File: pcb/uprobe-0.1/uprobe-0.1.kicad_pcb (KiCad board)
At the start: 4 copper layers, 33.5 x 77 mm, 103 parts, among them J1 uConsoleEXT, J2 Conn_02x05_Odd_Even, J3 Conn_02x05_Odd_Even, J4 JST_SH_BM03B-SRSS, J5 Conn_01x02, J7 Conn_01x04, Q1 BSS138, Q2 BSS138, Q3 BSS138, Q4 BSS138, Q5 BSS138, Q6 BSS138, Q7 DMG1024UV, Q8 DMG1023UV, SW1 XUNPU TS-1088-AR02016, SW2 XUNPU TS-1088-AR02016, U1 ATmega8A-M, U2 AMS1117-3.3, U3 AP22653, U4 AP22653, U5 STM32F103CBUx, U6 74LVC2T45DC, U7 74LVC2T45DC, U8 74LVC2T45DC, U9 74LVC2T45DC, Y1 ABM8-12.000MHZ-B2-T, Y2 ABM8-8.000MHZ-B2-T

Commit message: update usbasp schema
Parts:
- removed Q2, Q3, Q4, Q5, Q6: BSS138, Package_TO_SOT_SMD:SOT-23
- removed R11, R12, R13, R14, R15, R16, R17, R18, R19, R20: 10k, Resistor_SMD:R_0603_1608Metric
- removed R21, R22, R23, R24: 270, Resistor_SMD:R_0603_1608Metric
- added C29: 100n, Capacitor_SMD:C_0603_1608Metric, F.Cu at (136.7, 86.7)
- added C30: 100n, Capacitor_SMD:C_0603_1608Metric, F.Cu at (136.7, 82.5)
- added C31: 100n, Capacitor_SMD:C_0603_1608Metric, F.Cu at (136.6, 92.3)
- added C32: 100n, Capacitor_SMD:C_0603_1608Metric, F.Cu at (136.7, 88.2)
- added C33: 100n, Capacitor_SMD:C_0603_1608Metric, F.Cu at (136.7, 98.2)
- added C34: 100n, Capacitor_SMD:C_0603_1608Metric, F.Cu at (136.6, 93.9)
- added R37: 100, Resistor_SMD:R_0603_1608Metric, F.Cu at (141.1, 97.1)
- added R38: 100, Resistor_SMD:R_0603_1608Metric, F.Cu at (141.1, 86.6)
- added R39: 100, Resistor_SMD:R_0603_1608Metric, F.Cu at (141.1, 84.1)
- added R40: 100, Resistor_SMD:R_0603_1608Metric, F.Cu at (141.1, 89.2)
- added R41: 100, Resistor_SMD:R_0603_1608Metric, F.Cu at (141.1, 91.7)
- added R42: 100, Resistor_SMD:R_0603_1608Metric, F.Cu at (141.1, 94.3)
- added U10: 74LVC2T45DC, Package_SO:VSSOP-8_2.3x2mm_P0.5mm, F.Cu at (136.8, 84.6)
- added U11: 74LVC2T45DC, Package_SO:VSSOP-8_2.3x2mm_P0.5mm, F.Cu at (136.6, 90.3)
- added U12: 74LVC2T45DC, Package_SO:VSSOP-8_2.3x2mm_P0.5mm, F.Cu at (136.8, 96.2)
- moved J5 37.5 mm to (172.0, 92.1)
- moved R8 14.9 mm to (144.5, 76.3), turned to 90 degrees
- moved Q1 14.9 mm to (141.7, 76.3)
- moved R9 14.8 mm to (138.8, 76.3)
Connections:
- J2 pad 1: /UASP_MOSI -> Net-(J2-Pin_1)
- J2 pad 4: /UASP_TX -> Net-(J2-Pin_4)
- J2 pad 5: /UASP_RST -> Net-(J2-Pin_5)
- J2 pad 6: /UASP_RX -> Net-(J2-Pin_6)
- J2 pad 7: /UASP_SCK -> Net-(J2-Pin_7)
- J2 pad 9: /UASP_MISO -> Net-(J2-Pin_9)
- R8 pad 1: /UASP_RST -> /UASP_TARGET
- R8 pad 2: /UASP_TARGET -> /UASP_RST
- U1 pad 14: Net-(U1-PB2) -> /UASP_RST*
- U1 pad 15: Net-(U1-PB3) -> /UASP_MOSI*
- U1 pad 17: Net-(U1-PB5) -> /UASP_SCK*
- U1 pad 31: Net-(U1-PD1) -> /UASP_TX*

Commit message: layout update
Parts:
- added JP2: SolderJumper_3_Bridged12, Jumper:SolderJumper-3_P2.0mm_Open_TrianglePad1.0x1.5mm, B.Cu at (151.5, 117.9)
- added JP3: SolderJumper_2_Open, Jumper:SolderJumper-2_P1.3mm_Open_TrianglePad1.0x1.5mm, B.Cu at (146.6, 117.9)
- added LD3: XL-3210SURUGC, uprobe:XL-3210SURUGC, F.Cu at (150.4, 121.0)
- added LD4: XL-3210SURUGC, uprobe:XL-3210SURUGC, F.Cu at (150.4, 125.4)
- added R43: 270, Resistor_SMD:R_0603_1608Metric, F.Cu at (146.9, 119.7)
- added R44: 270, Resistor_SMD:R_0603_1608Metric, F.Cu at (146.9, 121.3)
- added R45: 270, Resistor_SMD:R_0603_1608Metric, F.Cu at (146.9, 125.1)
- added R46: 270, Resistor_SMD:R_0603_1608Metric, F.Cu at (146.9, 126.7)
- J4: moved to B.Cu
- moved Y2 70.5 mm to (129.9, 135.3)
- moved C19 60.6 mm to (129.9, 137.8), turned to 180 degrees
- moved R32 59.9 mm to (137.1, 137.5), turned to 90 degrees
- moved U9 58.7 mm to (139.1, 107.3)
- moved C7 57.6 mm to (129.6, 117.1)
- moved C13 57.0 mm to (125.7, 132.4), turned to 180 degrees
- moved U7 56.1 mm to (139.1, 111.8)
- moved U8 55.9 mm to (139.2, 116.2)
- moved C20 55.6 mm to (132.8, 135.3), turned to 90 degrees
- moved R31 54.9 mm to (136.8, 121.3), turned to 180 degrees
- moved R28 54.6 mm to (131.1, 120.6), turned to -90 degrees
- moved R27 53.4 mm to (132.6, 120.6), turned to 90 degrees
- moved C16 53.0 mm to (125.7, 127.3), turned to 180 degrees
- moved C12 52.6 mm to (135.4, 137.5), turned to -90 degrees
- moved JP1 51.9 mm to (125.7, 129.8), turned to 90 degrees
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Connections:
- net /UASP_MISO renamed /xUASP_MISO
- net /UASP_MISO* renamed /iUASP_MISO
- net /UASP_MOSI renamed /xUASP_MOSI
- net /UASP_MOSI* renamed /iUASP_MOSI
- net /UASP_RST renamed /xUASP_RST
- net /UASP_RST* renamed /iUASP_RST
- net /UASP_RX renamed /xUASP_RX
- net /UASP_RX* renamed /iUASP_RX
- net /UASP_SCK renamed /xUASP_SCK
- net /UASP_SCK* renamed /iUASP_SCK
- net /UASP_TX renamed /xUASP_TX
- net /UASP_TX* renamed /iUASP_TX
- net Net-(U5-PB0) renamed /TPWR_DTCT
- J3 pad 7: unconnected-(J3-Pin_7-Pad7) -> Net-(J3-Pin_7)
- J3 pad 9: GND -> Net-(J3-Pin_9)
- RN1 pad 1: /xTDI -> /TDI
- RN1 pad 2: /xTDO -> /TDO
- RN1 pad 3: /xTCK -> /TCK
- RN1 pad 4: /xTMS -> /TMS
- RN1 pad 5: /TMS -> /xTMS
- RN1 pad 6: /TCK -> /xTCK
- RN1 pad 7: /TDO -> /xTDO
- RN1 pad 8: /TDI -> /xTDI
- RN2 pad 1: /xTXD -> /TXD
- RN2 pad 2: /xRXD -> /RXD
- RN2 pad 3: /xTPWR -> /RST
- RN2 pad 4: /xRST -> /TPWR
- RN2 pad 5: /RST -> /xTPWR
- RN2 pad 6: /TPWR -> /xRST
- RN2 pad 7: /RXD -> /xRXD
- RN2 pad 8: /TXD -> /xTXD
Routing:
- net +5V: track 13.6 -> 12.6 mm
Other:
- board text added: "github.com xx0x/uprobe"
- board text added: "swd/jtag"
- board text added: "uart"
- board text added: "uprobe 0.1"
- board text added: "usbasp"

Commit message: routing
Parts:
- moved F1 2.80 mm to (125.2, 86.2)
- moved J5 2.50 mm to (135.2, 101.0), turned to 90 degrees
- moved R10 0.40 mm to (127.8, 98.6)
- moved C11 0.30 mm to (127.7, 92.8)
- moved U4 0.30 mm to (127.7, 95.7)
- moved R5 0.20 mm to (149.0, 75.8)
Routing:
- net +5V: track 12.6 -> 129.3 mm, vias 0 -> 6
- net /UASP_TARGET: track 0.00 -> 75.9 mm, vias 0 -> 6
- net /SPK_RN: track 0.00 -> 74.8 mm, vias 0 -> 2
- net /SPK_RP: track 0.00 -> 69.8 mm, vias 0 -> 2
- net +3V3: track 6.07 -> 67.4 mm, vias 0 -> 4
- net /~{UASP_SLOW_SCK}: track 0.00 -> 52.7 mm, vias 0 -> 1
- net /SPK_LN: track 0.00 -> 50.8 mm, vias 0 -> 1
- net /SPK_LP: track 0.00 -> 45.6 mm, vias 0 -> 3
- net /~{UASP_POWER_FAULT}: track 0.00 -> 39.3 mm, vias 0 -> 1
- net /USB3_D+: track 0.00 -> 35.1 mm
- net /USB3_D-: track 0.00 -> 34.2 mm
- net /iUASP_RX: track 0.00 -> 34.0 mm, vias 0 -> 2
- net /iUASP_MISO: track 0.00 -> 30.0 mm, vias 0 -> 2
- net /USB4_D+: track 0.00 -> 28.1 mm, vias 0 -> 2
- net /USB4_D-: track 0.00 -> 28.0 mm, vias 0 -> 2
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
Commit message: routing
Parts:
- moved C14 1.05 mm to (138.6, 124.3)
- moved Q7 0.50 mm to (139.7, 131.6)
- moved R35 0.49 mm to (141.7, 131.1)
- moved SW2 0.20 mm to (140.1, 136.0)
- moved C16 0.15 mm to (125.7, 127.5)
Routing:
- net GND: track 8.16 -> 220.5 mm, vias 0 -> 100
- net +3V3: track 67.4 -> 181.4 mm, vias 4 -> 10
- net /iTMS_DIR: track 0.00 -> 44.2 mm, vias 0 -> 2
- net /iTDO: track 0.00 -> 42.6 mm, vias 0 -> 3
- net /xTPWR: track 2.06 -> 43.9 mm, vias 0 -> 5
- net /PWR_BR: track 3.29 -> 37.8 mm, vias 0 -> 2
- net /~{BM_RST}: track 0.00 -> 30.2 mm, vias 0 -> 1
- net /iTMS: track 0.00 -> 26.8 mm, vias 0 -> 2
- net /iTDI: track 0.00 -> 21.9 mm, vias 0 -> 2
- net +5V: track 129.3 -> 151.0 mm, vias 6 -> 8
- net /iTCK: track 0.00 -> 21.6 mm, vias 0 -> 2
- net Net-(U5-PB12): track 0.00 -> 20.9 mm, vias 0 -> 2
- net /xRST: track 0.00 -> 20.9 mm, vias 0 -> 2
- net /TPWR: track 5.36 -> 25.7 mm, vias 0 -> 3
- net (no net): track 18.9 -> 0.00 mm
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- added copper zone on B.Cu, net GND
- added copper zone on F.Cu, net GND
- added copper zone on In1.Cu, net GND
- added copper zone on In2.Cu, net GND

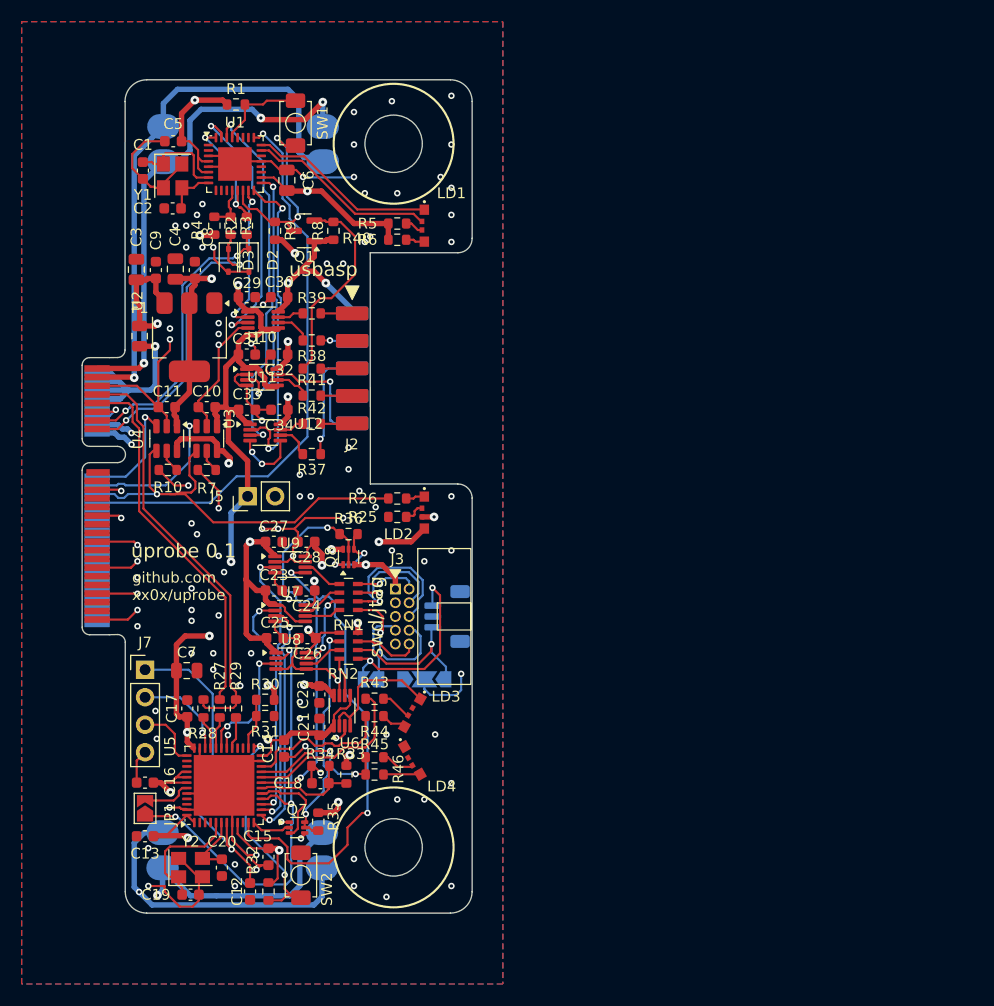
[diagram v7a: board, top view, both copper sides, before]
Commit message: routing cleanup
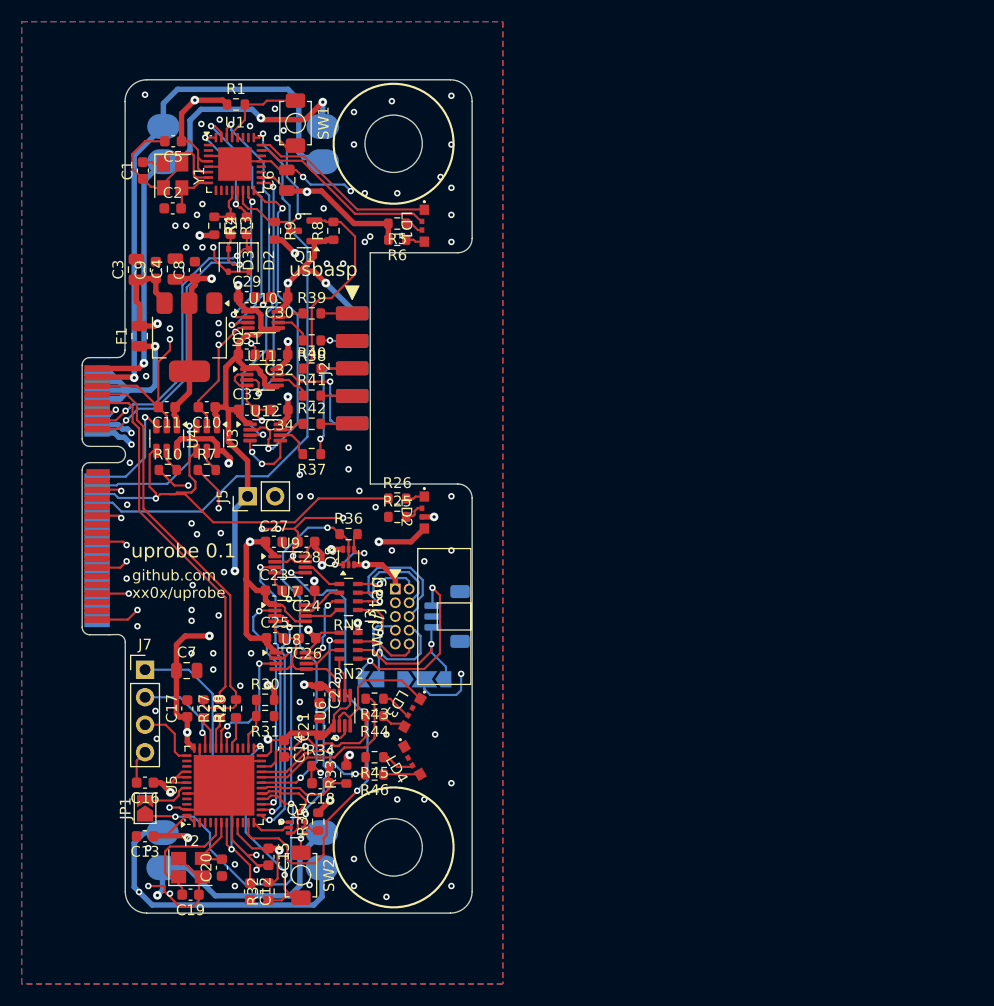
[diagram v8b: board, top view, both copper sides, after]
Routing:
- net +3V3: track 181.4 -> 183.5 mm
- net /PWR_BR: track 37.8 -> 36.3 mm
- net /~{BM_RST}: track 30.2 -> 28.9 mm
- net /iUASP_MISO: track 30.3 -> 31.5 mm
- net GND: track 220.5 -> 219.2 mm, vias 100 -> 112
- net +5V: track 151.0 -> 152.2 mm
- net /xTPWR: track 43.9 -> 42.8 mm
- net /iTDO: track 42.6 -> 43.5 mm
- net /iUASP_RX: track 34.2 -> 35.0 mm
- net /~{UASP_SLOW_SCK}: track 52.7 -> 53.3 mm
